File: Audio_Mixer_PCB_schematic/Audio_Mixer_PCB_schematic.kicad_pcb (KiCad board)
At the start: 2 copper layers, 1.4 x 13 mm, 77 parts, among them J7 AudioJack3_SwitchTR, J8 AudioJack3_SwitchTR, J9 AudioJack3_SwitchTR, SW1 SW_SPST, U1 TL074, U2 TL074, U3 TL074, U4 TL074

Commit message: more routing. saved to transfer to other pc.
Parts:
- moved R30 112.5 mm to (80.0, 93.0)
- moved C13 74.3 mm to (75.5, 97.5)
- moved R22 48.2 mm to (76.0, 121.5)
- moved C9 29.7 mm to (66.5, 97.5)
- moved C3 24.9 mm to (71.0, 121.5)
- moved C10 22.3 mm to (71.0, 97.5)
- moved C14 18.0 mm to (75.5, 93.0)
- moved R27 16.6 mm to (66.5, 93.0)
- moved SW1 14.3 mm to (170.5, 129.0)
- moved BT1 14.0 mm to (183.0, 129.0), turned to 90 degrees
- moved U1 12.7 mm to (75.0, 105.0), turned to -90 degrees
- moved R21 11.6 mm to (69.0, 116.5)
- moved R4 10.7 mm to (174.5, 117.5), turned to 90 degrees
- moved R42 10.3 mm to (154.0, 127.0)
- moved C1 8.50 mm to (169.5, 117.5), turned to 90 degrees
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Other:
- board text added: "Battery"

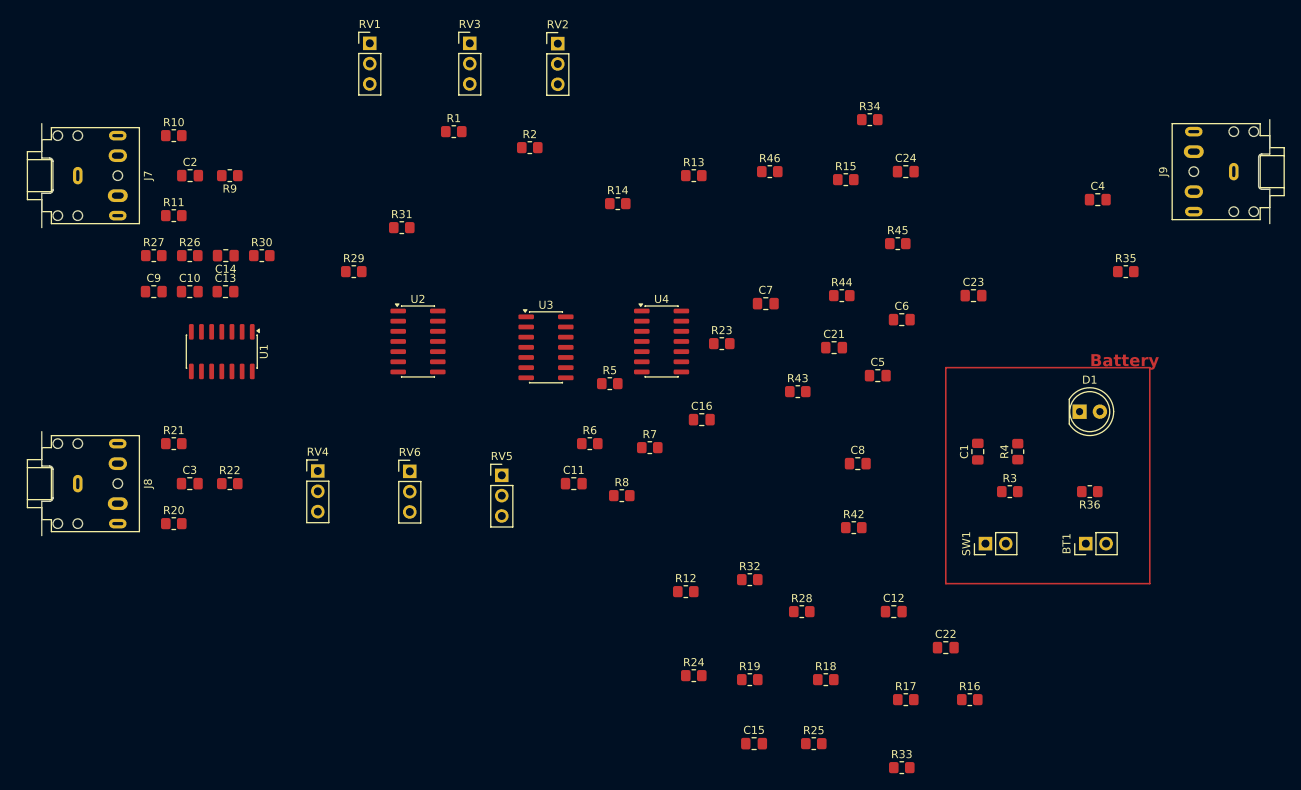
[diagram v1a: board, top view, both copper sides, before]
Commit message: routed all traces, moved components to better looking areas, fixed all DRC errors
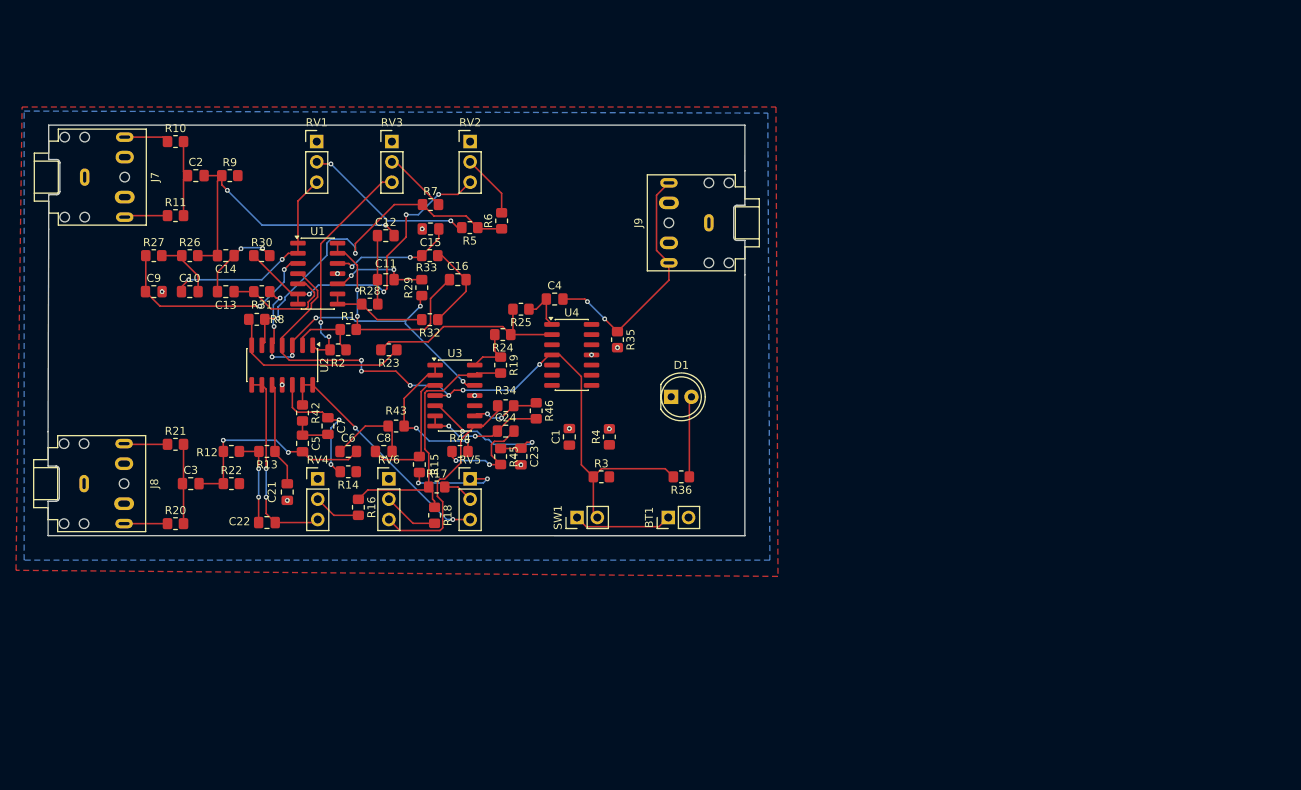
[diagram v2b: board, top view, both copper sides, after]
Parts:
- moved R33 87.0 mm to (101.0, 93.0)
- moved C22 86.3 mm to (80.6, 126.4), turned to 180 degrees
- moved R16 80.1 mm to (92.1, 124.5), turned to -90 degrees
- moved C12 79.0 mm to (95.5, 90.5)
- moved C15 76.0 mm to (101.1, 89.7), turned to 180 degrees
- moved C5 72.4 mm to (85.1, 116.5), turned to -90 degrees
- moved C6 71.1 mm to (90.8, 117.5)
- moved C21 70.7 mm to (83.2, 122.6), turned to -90 degrees
- moved R42 70.4 mm to (85.1, 112.7), turned to -90 degrees
- moved C4 69.0 mm to (116.6, 98.4)
- moved R28 66.3 mm to (93.5, 99.1)
- moved J9 65.9 mm to (135.9, 88.9)
- moved R25 65.5 mm to (112.4, 99.7), turned to 180 degrees
- moved R17 64.4 mm to (101.9, 121.9)
- moved R35 64.1 mm to (124.5, 103.5), turned to -90 degrees
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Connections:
- C15 pad 2: 0 -> GND
- C21 pad 2: 0 -> GND
- C23 pad 2: 0 -> GND
- C9 pad 2: 0 -> GND
- R23 pad 1: Net-(U4A--) -> Net-(R23-Pad1)
- R23 pad 2: Net-(R23-Pad2) -> Net-(U4A--)
- R8 pad 1: Net-(R23-Pad2) -> Net-(R23-Pad1)
- U2 pad 7: Net-(R23-Pad2) -> Net-(R23-Pad1)
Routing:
- net +9V: track 0.00 -> 87.6 mm, vias 0 -> 6
- net VRef: track 0.00 -> 58.0 mm, vias 0 -> 9
- net Net-(U2B--): track 0.00 -> 44.8 mm, vias 0 -> 2
- net Net-(U1B--): track 0.00 -> 40.8 mm, vias 0 -> 4
- net Net-(C12-Pad2): track 0.00 -> 40.4 mm, vias 0 -> 2
- net Net-(U3D--): track 0.00 -> 34.7 mm
- net Net-(C4-Pad2): track 0.00 -> 31.1 mm, vias 0 -> 2
- net Net-(U2D--): track 0.00 -> 30.5 mm, vias 0 -> 2
- net Net-(R2-Pad2): track 0.00 -> 28.6 mm, vias 0 -> 2
- net Net-(U1D--): track 0.00 -> 28.5 mm, vias 0 -> 2
- net Net-(U1A-+): track 0.00 -> 27.4 mm, vias 0 -> 2
- net Net-(R34-Pad2): track 0.00 -> 27.0 mm
- net Net-(U1A--): track 0.00 -> 26.7 mm, vias 0 -> 2
- net Net-(C3-Pad2): track 0.00 -> 26.6 mm, vias 0 -> 2
- net Net-(U4A--): track 0.00 -> 26.3 mm
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- added copper zone on B.Cu, net GND
- added copper zone on F.Cu, net VRef
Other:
- board size 1.4 x 13 mm -> 87.1 x 51.3 mm
- board text removed: "Battery"
